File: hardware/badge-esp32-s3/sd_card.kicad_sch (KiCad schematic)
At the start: 2 parts, among them J4 Micro_SD_Card

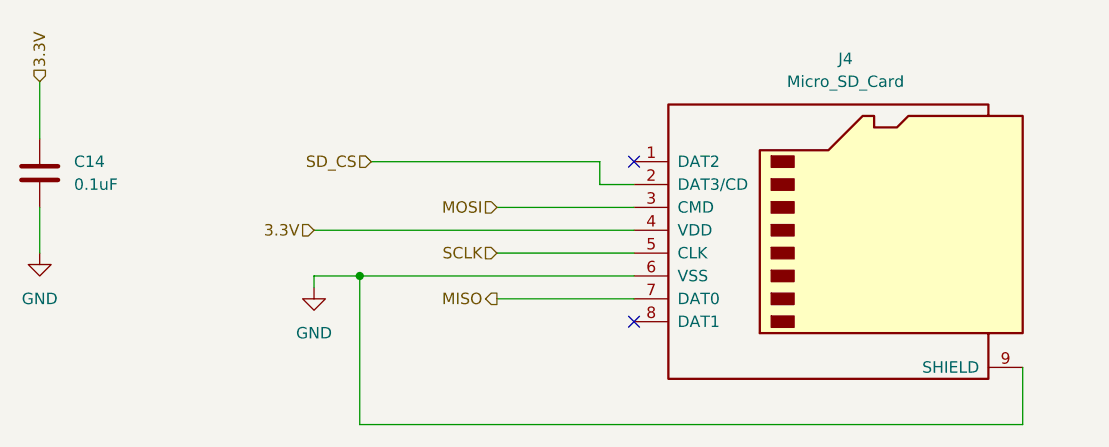
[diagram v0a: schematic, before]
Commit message: Update sd_card.kicad_sch
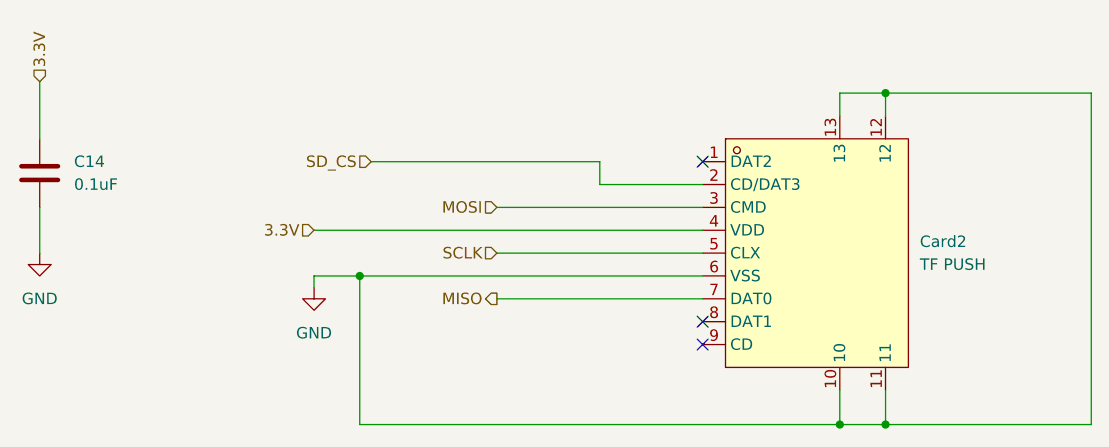
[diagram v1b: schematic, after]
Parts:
- removed J4: Micro_SD_Card, symbol Connector:Micro_SD_Card
- added Card2: TF PUSH, lcsc-lib:TF-SMD_TF-PUSH, symbol lcsc-lib:TFPUSH
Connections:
- net 3.3V: now also Card2.4 (VDD)
- net GND: now also Card2.10, Card2.11, Card2.12, Card2.13, Card2.6 (VSS)
- net MISO: now also Card2.7 (DAT0)
- net MOSI: now also Card2.3 (CMD)
- net SCLK: now also Card2.5 (CLX)
- net SD_CS: now also Card2.2 (CD/DAT3)
- no-connect marks 2 -> 3
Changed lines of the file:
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@@
 	(paper "A4")
+	(junction
+		(at 193.04 39.37)
+		(diameter 0)
+		(color 0 0 0 0)
+	)
 	(junction
 		(at 134.62 59.69)
@@
 		(color 0 0 0 0)
 	)
+	(junction
+		(at 193.04 76.2)
+		(diameter 0)
+		(color 0 0 0 0)
+	)
+	(junction
+		(at 187.96 76.2)
+		(diameter 0)
+		(color 0 0 0 0)
+	)
 	(no_connect
-		(at 165.1 46.99)
+		(at 172.72 46.99)
 	)
 	(no_connect
-		(at 165.1 64.77)
+		(at 172.72 64.77)
+	)
+	(no_connect
+		(at 172.72 67.31)
 	)
 	(wire
@@
 	(wire
 		(pts
-			(xy 129.54 54.61) (xy 165.1 54.61)
-		)
-		(stroke
-			(width 0)
-			(type default)
-		)
-	)
-	(wire
-		(pts
-			(xy 208.28 69.85) (xy 208.28 76.2)
-		)
-		(stroke
-			(width 0)
-			(type default)
-		)
-	)
-	(wire
-		(pts
-			(xy 161.29 46.99) (xy 161.29 49.53)
-		)
-		(stroke
-			(width 0)
-			(type default)
-		)
-	)
-	(wire
-		(pts
-			(xy 134.62 59.69) (xy 165.1 59.69)
-		)
-		(stroke
-			(width 0)
-			(type default)
-		)
-	)
-	(wire
-		(pts
-			(xy 149.86 52.07) (xy 165.1 52.07)
+			(xy 187.96 72.39) (xy 187.96 76.2)
+		)
+		(stroke
+			(width 0)
+			(type default)
+		)
+	)
+	(wire
+		(pts
+			(xy 193.04 39.37) (xy 193.04 41.91)
+		)
+		(stroke
+			(width 0)
+			(type default)
+		)
+	)
+	(wire
+		(pts
+			(xy 129.54 54.61) (xy 172.72 54.61)
+		)
+		(stroke
+			(width 0)
+			(type default)
+		)
+	)
+	(wire
+		(pts
+			(xy 193.04 39.37) (xy 187.96 39.37)
+		)
+		(stroke
+			(width 0)
+			(type default)
+		)
+	)
+	(wire
+		(pts
+			(xy 187.96 76.2) (xy 134.62 76.2)
+		)
+		(stroke
+			(width 0)
+			(type default)
+		)
+	)
+	(wire
+		(pts
+			(xy 215.9 39.37) (xy 193.04 39.37)
+		)
+		(stroke
+			(width 0)
+			(type default)
+		)
+	)
+	(wire
+		(pts
+			(xy 193.04 76.2) (xy 187.96 76.2)
+		)
+		(stroke
+			(width 0)
+			(type default)
+		)
+	)
+	(wire
+		(pts
+			(xy 161.29 49.53) (xy 161.29 46.99)
+		)
+		(stroke
+			(width 0)
+			(type default)
+		)
+	)
+	(wire
+		(pts
+			(xy 134.62 59.69) (xy 172.72 59.69)
+		)
+		(stroke
+			(width 0)
+			(type default)
+		)
+	)
+	(wire
+		(pts
+			(xy 149.86 52.07) (xy 172.72 52.07)
 		)
 		(stroke
@@
 	(wire
 		(pts
+			(xy 187.96 39.37) (xy 187.96 41.91)
+		)
+		(stroke
+			(width 0)
+			(type default)
+		)
+	)
+	(wire
+		(pts
 			(xy 99.06 38.1) (xy 99.06 44.45)
 		)
@@
 	(wire
 		(pts
+			(xy 193.04 72.39) (xy 193.04 76.2)
+		)
+		(stroke
+			(width 0)
+			(type default)
+		)
+	)
+	(wire
+		(pts
+			(xy 215.9 39.37) (xy 215.9 76.2)
+		)
+		(stroke
+			(width 0)
+			(type default)
+		)
+	)
+	(wire
+		(pts
 			(xy 134.62 76.2) (xy 134.62 59.69)
 		)
@@
 	(wire
 		(pts
-			(xy 208.28 76.2) (xy 134.62 76.2)
-		)
-		(stroke
-			(width 0)
-			(type default)
-		)
-	)
-	(wire
-		(pts
-			(xy 149.86 57.15) (xy 165.1 57.15)
-		)
-		(stroke
-			(width 0)
-			(type default)
-		)
-	)
-	(wire
-		(pts
-			(xy 161.29 49.53) (xy 165.1 49.53)
-		)
-		(stroke
-			(width 0)
-			(type default)
-		)
-	)
-	(wire
-		(pts
-			(xy 149.86 62.23) (xy 165.1 62.23)
+			(xy 215.9 76.2) (xy 193.04 76.2)
+		)
+		(stroke
+			(width 0)
+			(type default)
+		)
+	)
+	(wire
+		(pts
+			(xy 149.86 57.15) (xy 172.72 57.15)
+		)
+		(stroke
+			(width 0)
+			(type default)
+		)
+	)
+	(wire
+		(pts
+			(xy 161.29 49.53) (xy 172.72 49.53)
+		)
+		(stroke
+			(width 0)
+			(type default)
+		)
+	)
+	(wire
+		(pts
+			(xy 149.86 62.23) (xy 172.72 62.23)
 		)
 		(stroke
@@
 			)
 			(justify right)
+		)
+	)
+	(symbol
+		(lib_id "lcsc-lib:TFPUSH")
+		(at 182.88 57.15 0)
+		(unit 1)
+		(exclude_from_sim no)
+		(in_bom yes)
+		(on_board yes)
+		(dnp no)
+		(fields_autoplaced yes)
+		(property "Reference" "Card2"
+			(at 196.85 55.8799 0)
+			(effects
+				(font
+					(size 1.27 1.27)
+				)
+				(justify left)
+			)
+		)
+		(property "Value" "TF PUSH"
+			(at 196.85 58.4199 0)
+			(effects
+				(font
+					(size 1.27 1.27)
+				)
+				(justify left)
+			)
+		)
+		(property "Footprint" "lcsc-lib:TF-SMD_TF-PUSH"
+			(at 182.88 80.01 0)
+			(effects
+				(font
+					(size 1.27 1.27)
+				)
+				(hide yes)
+			)
+		)
+		(property "Datasheet" "https://lcsc.com/product-detail/Connector-Card-Sockets_SHOU-HAN-SHOU-HAN-TFDeck-TF-Deck_C393941.html"
+			(at 182.88 82.55 0)
+			(effects
+				(font
+					(size 1.27 1.27)
+				)
+				(hide yes)
+			)
+		)
+		(property "Description" ""
+			(at 182.88 57.15 0)
+			(effects
+				(font
+					(size 1.27 1.27)
+				)
+				(hide yes)
+			)
+		)
+		(property "LCSC Part" "C393941"
+			(at 182.88 85.09 0)
+			(effects
+				(font
+					(size 1.27 1.27)
+				)
+				(hide yes)
+			)
+		)
+		(pin "11"
+		)
+		(pin "10"
+		)
+		(pin "12"
+		)
+		(pin "8"
+		)
+		(pin "9"
+		)
+		(pin "7"
+		)
+		(pin "13"
+		)
+		(pin "6"
+		)
+		(pin "1"
+		)
+		(pin "2"
+		)
+		(pin "3"
+		)
+		(pin "4"
+		)
+		(pin "5"
+		)
+		(instances
+			(project ""
+				(path "/e2af9a6c-dbe9-4de2-9ba6-ea213a7300ec/61971e93-08b4-4717-9ec8-ac07d8e404d2"
+					(reference "Card2")
+					(unit 1)
+				)
+			)
 		)
 	)
@@
 					(unit 1)
 				)
-			)
-		)
-	)
-	(symbol
-		(lib_id "Connector:Micro_SD_Card")
-		(at 187.96 54.61 0)
-		(unit 1)
-		(exclude_from_sim no)
-		(in_bom yes)
-		(on_board yes)
-		(dnp no)
-		(fields_autoplaced yes)
-		(property "Reference" "J4"
-			(at 188.595 35.56 0)
-			(effects
-				(font
-					(size 1.27 1.27)
-				)
-			)
-		)
-		(property "Value" "Micro_SD_Card"
-			(at 188.595 38.1 0)
-			(effects
-				(font
-					(size 1.27 1.27)
-				)
-			)
-		)
-		(property "Footprint" ""
-			(at 217.17 46.99 0)
-			(effects
-				(font
-					(size 1.27 1.27)
-				)
-				(hide yes)
-			)
-		)
-		(property "Datasheet" "https://www.we-online.com/components/products/datasheet/693072010801.pdf"
-			(at 187.96 54.61 0)
-			(effects
-				(font
-					(size 1.27 1.27)
-				)
-				(hide yes)
-			)
-		)
-		(property "Description" "Micro SD Card Socket"
-			(at 187.96 54.61 0)
-			(effects
-				(font
-					(size 1.27 1.27)
-				)
-				(hide yes)
-			)
-		)
-		(pin "4"
-		)
-		(pin "6"
-		)
-		(pin "1"
-		)
-		(pin "9"
-		)
-		(pin "2"
-		)
-		(pin "5"
-		)
-		(pin "7"
-		)
-		(pin "8"
-		)
-		(pin "3"
-		)
-		(instances
-			(project ""
-				(path "/e2af9a6c-dbe9-4de2-9ba6-ea213a7300ec/61971e93-08b4-4717-9ec8-ac07d8e404d2"
-					(reference "J4")
-					(unit 1)
-				)

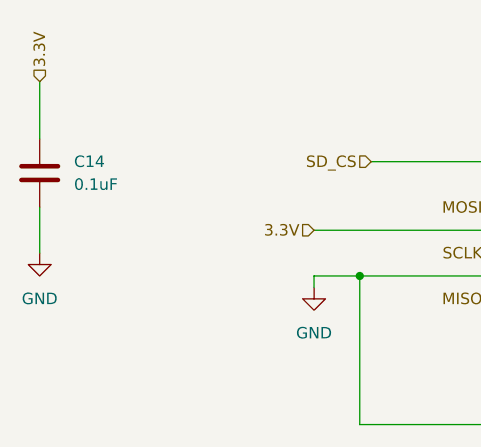
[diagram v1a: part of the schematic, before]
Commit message: Fleshed out schematic with all exposed pins
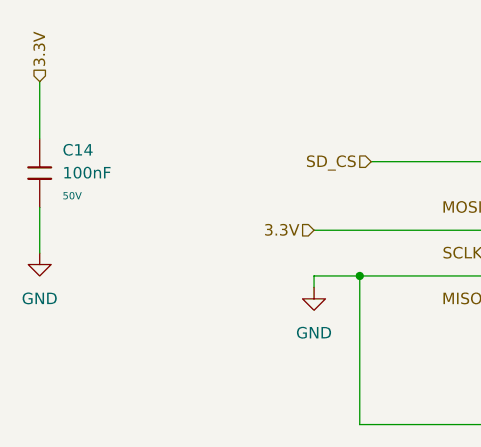
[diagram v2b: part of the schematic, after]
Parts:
- C14: value 0.1uF -> 100nF; footprint Capacitor_SMD:C_0603_1608Metric -> PCM_JLCPCB:C_0603; symbol Device:C -> PCM_JLCPCB-Capacitors:0603,100nF; Attrition Qty (none) -> 10; Capacitance (none) -> 100nF; Category (none) -> Capacitors,Multilayer Ceramic Capacitors MLCC - SMD/SMT; Class (none) -> Basic Component; LCSC (none) -> C14663; Manufacturer (none) -> YAGEO; Minimum Qty (none) -> 20; Part (none) -> CC0603KRX7R9BB104; Price (none) -> 0.006USD; Process (none) -> SMT; Stock (none) -> 83501114; Temperature Coefficient (none) -> X7R; Tolerance (none) -> ±10%; Voltage Rated (none) -> 50V
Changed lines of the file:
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@@
 	)
 	(symbol
-		(lib_id "Device:C")
+		(lib_id "PCM_JLCPCB-Capacitors:0603,100nF")
 		(at 99.06 48.26 0)
 		(unit 1)
@@
 		(fields_autoplaced yes)
 		(property "Reference" "C14"
-			(at 102.87 46.9899 0)
+			(at 101.6 45.7199 0)
 			(effects
 				(font
@@
 			)
 		)
-		(property "Value" "0.1uF"
-			(at 102.87 49.5299 0)
+		(property "Value" "100nF"
+			(at 101.6 48.2599 0)
 			(effects
 				(font
@@
 			)
 		)
-		(property "Footprint" "Capacitor_SMD:C_0603_1608Metric"
-			(at 100.0252 52.07 0)
+		(property "Footprint" "PCM_JLCPCB:C_0603"
+			(at 97.282 48.26 90)
 			(effects
 				(font
@@
 			)
 		)
-		(property "Datasheet" "~"
+		(property "Datasheet" "https://www.lcsc.com/datasheet/lcsc_datasheet_2211101700_YAGEO-CC0603KRX7R9BB104_C14663.pdf"
 			(at 99.06 48.26 0)
 			(effects
@@
 			)
 		)
-		(property "Description" "Unpolarized capacitor"
+		(property "Description" "50V 100nF X7R ±10% 0603 Multilayer Ceramic Capacitors MLCC - SMD/SMT ROHS"
 			(at 99.06 48.26 0)
 			(effects
+				(font
+					(size 1.27 1.27)
+				)
+				(hide yes)
+			)
+		)
+		(property "LCSC" "C14663"
+			(at 99.06 48.26 0)
+			(effects
+				(font
+					(size 1.27 1.27)
+				)
+				(hide yes)
+			)
+		)
+		(property "Stock" "83501114"
+			(at 99.06 48.26 0)
+			(effects
+				(font
+					(size 1.27 1.27)
+				)
+				(hide yes)
+			)
+		)
+		(property "Price" "0.006USD"
+			(at 99.06 48.26 0)
+			(effects
+				(font
+					(size 1.27 1.27)
+				)
+				(hide yes)
+			)
+		)
+		(property "Process" "SMT"
+			(at 99.06 48.26 0)
+			(effects
+				(font
+					(size 1.27 1.27)
+				)
+				(hide yes)
+			)
+		)
+		(property "Minimum Qty" "20"
+			(at 99.06 48.26 0)
+			(effects
+				(font
+					(size 1.27 1.27)
+				)
+				(hide yes)
+			)
+		)
+		(property "Attrition Qty" "10"
+			(at 99.06 48.26 0)
+			(effects
+				(font
+					(size 1.27 1.27)
+				)
+				(hide yes)
+			)
+		)
+		(property "Class" "Basic Component"
+			(at 99.06 48.26 0)
+			(effects
+				(font
+					(size 1.27 1.27)
+				)
+				(hide yes)
+			)
+		)
+		(property "Category" "Capacitors,Multilayer Ceramic Capacitors MLCC - SMD/SMT"
+			(at 99.06 48.26 0)
+			(effects
+				(font
+					(size 1.27 1.27)
+				)
+				(hide yes)
+			)
+		)
+		(property "Manufacturer" "YAGEO"
+			(at 99.06 48.26 0)
+			(effects
+				(font
+					(size 1.27 1.27)
+				)
+				(hide yes)
+			)
+		)
+		(property "Part" "CC0603KRX7R9BB104"
+			(at 99.06 48.26 0)
+			(effects
+				(font
+					(size 1.27 1.27)
+				)
+				(hide yes)
+			)
+		)
+		(property "Voltage Rated" "50V"
+			(at 101.6 50.8 0)
+			(effects
+				(font
+					(size 0.8 0.8)
+				)
+				(justify left)
+			)
+		)
+		(property "Tolerance" "±10%"
+			(at 99.06 48.26 0)
+			(effects
+				(font
+					(size 1.27 1.27)
+				)
+				(hide yes)
+			)
+		)
+		(property "Capacitance" "100nF"
+			(at 99.06 48.26 0)
+			(effects
+				(font
+					(size 1.27 1.27)
+				)
+				(hide yes)
+			)
+		)
+		(property "Temperature Coefficient" "X7R"
+			(at 99.06 48.26 0)
+			(effects

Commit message: Annotate schematic
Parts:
- renumbered Card2 to Card1
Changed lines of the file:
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@@
 		(dnp no)
 		(fields_autoplaced yes)
-		(property "Reference" "Card2"
+		(property "Reference" "Card1"
 			(at 196.85 55.8799 0)
 			(effects
@@
 			(project ""
 				(path "/e2af9a6c-dbe9-4de2-9ba6-ea213a7300ec/61971e93-08b4-4717-9ec8-ac07d8e404d2"
-					(reference "Card2")
+					(reference "Card1")
 					(unit 1)
 				)
@@
 		(dnp no)
 		(fields_autoplaced yes)
-		(property "Reference" "#PWR031"
+		(property "Reference" "#PWR042"
 			(at 129.54 67.31 0)
 			(effects
@@
 			(project ""
 				(path "/e2af9a6c-dbe9-4de2-9ba6-ea213a7300ec/61971e93-08b4-4717-9ec8-ac07d8e404d2"
-					(reference "#PWR031")
+					(reference "#PWR042")
 					(unit 1)
 				)
@@
 		(dnp no)
 		(fields_autoplaced yes)
-		(property "Reference" "#PWR038"
+		(property "Reference" "#PWR041"
 			(at 99.06 63.5 0)
 			(effects
@@
 			(project ""
 				(path "/e2af9a6c-dbe9-4de2-9ba6-ea213a7300ec/61971e93-08b4-4717-9ec8-ac07d8e404d2"
-					(reference "#PWR038")
+					(reference "#PWR041")
 					(unit 1)
 				)
